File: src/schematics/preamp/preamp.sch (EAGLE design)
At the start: 33 parts

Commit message: Added input protection resistor to preamp
Ah input resistor was added to preamp inputs, so that short circuits of
clamping diodes won't hurt the connected device outputs.

Andrea Zoppi
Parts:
- added R17, R18: 1k, rcl:R-US_0204/5
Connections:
- new net N$3: C3.-, D3.A, D4.C, R18.2, R2.2
- new net N$8: C2.-, D1.A, D2.C, R17.2, R4.2
- net INA: now also R17.1; no longer C2.-, D1.A, D2.C, R4.2
- net INB: now also R18.1; no longer C3.-, D3.A, D4.C, R2.2
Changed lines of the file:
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@@
 <part name="C8" library="rcl" deviceset="C-US" device="050-025X075" value="47n"/>
 <part name="C1" library="rcl" deviceset="CPOL-US" device="E2-4" value="1u5"/>
+<part name="R17" library="rcl" deviceset="R-US_" device="0204/5" value="1k"/>
+<part name="R18" library="rcl" deviceset="R-US_" device="0204/5" value="1k"/>
 </parts>
 <sheets>
@@
 <instance part="C8" gate="G$1" x="7.62" y="144.78"/>
 <instance part="C1" gate="G$1" x="17.78" y="144.78"/>
+<instance part="R17" gate="G$1" x="-2.54" y="96.52"/>
+<instance part="R18" gate="G$1" x="-2.54" y="50.8"/>
 </instances>
 <busses>
@@
 <net name="INA" class="0">
 <segment>
-<pinref part="R4" gate="G$1" pin="2"/>
-<wire x1="12.7" y1="96.52" x2="5.08" y2="96.52" width="0.1524" layer="91"/>
-<wire x1="5.08" y1="96.52" x2="5.08" y2="93.98" width="0.1524" layer="91"/>
-<wire x1="12.7" y1="91.44" x2="12.7" y2="96.52" width="0.1524" layer="91"/>
-<wire x1="12.7" y1="101.6" x2="12.7" y2="96.52" width="0.1524" layer="91"/>
-<junction x="12.7" y="96.52"/>
-<wire x1="-5.08" y1="96.52" x2="5.08" y2="96.52" width="0.1524" layer="91"/>
-<junction x="5.08" y="96.52"/>
-<label x="-2.54" y="96.52" size="1.778" layer="95"/>
-<pinref part="D1" gate="G$1" pin="A"/>
-<pinref part="D2" gate="G$1" pin="C"/>
-<wire x1="20.32" y1="96.52" x2="12.7" y2="96.52" width="0.1524" layer="91"/>
-<pinref part="C2" gate="G$1" pin="-"/>
+<pinref part="R17" gate="G$1" pin="1"/>
+<wire x1="-7.62" y1="96.52" x2="-17.78" y2="96.52" width="0.1524" layer="91"/>
+<label x="-15.24" y="96.52" size="1.778" layer="95"/>
 </segment>
 </net>
@@
 <net name="INB" class="0">
 <segment>
-<wire x1="12.7" y1="55.88" x2="12.7" y2="50.8" width="0.1524" layer="91"/>
-<pinref part="R2" gate="G$1" pin="2"/>
-<wire x1="12.7" y1="50.8" x2="12.7" y2="45.72" width="0.1524" layer="91"/>
-<wire x1="12.7" y1="50.8" x2="5.08" y2="50.8" width="0.1524" layer="91"/>
-<wire x1="5.08" y1="50.8" x2="5.08" y2="48.26" width="0.1524" layer="91"/>
-<junction x="12.7" y="50.8"/>
-<wire x1="-5.08" y1="50.8" x2="5.08" y2="50.8" width="0.1524" layer="91"/>
-<junction x="5.08" y="50.8"/>
-<label x="-2.54" y="50.8" size="1.778" layer="95"/>
-<pinref part="D3" gate="G$1" pin="A"/>
-<pinref part="D4" gate="G$1" pin="C"/>
-<pinref part="C3" gate="G$1" pin="-"/>
-<wire x1="20.32" y1="50.8" x2="12.7" y2="50.8" width="0.1524" layer="91"/>
+<pinref part="R18" gate="G$1" pin="1"/>
+<wire x1="-7.62" y1="50.8" x2="-17.78" y2="50.8" width="0.1524" layer="91"/>
+<label x="-15.24" y="50.8" size="1.778" layer="95"/>
 </segment>
 </net>
@@
 </segment>
 </net>
+<net name="N$3" class="0">
+<segment>
+<pinref part="R18" gate="G$1" pin="2"/>
+<pinref part="C3" gate="G$1" pin="-"/>
+<wire x1="2.54" y1="50.8" x2="5.08" y2="50.8" width="0.1524" layer="91"/>
+<pinref part="D3" gate="G$1" pin="A"/>
+<wire x1="5.08" y1="50.8" x2="12.7" y2="50.8" width="0.1524" layer="91"/>
+<wire x1="12.7" y1="50.8" x2="20.32" y2="50.8" width="0.1524" layer="91"/>
+<wire x1="12.7" y1="55.88" x2="12.7" y2="50.8" width="0.1524" layer="91"/>
+<pinref part="D4" gate="G$1" pin="C"/>
+<wire x1="12.7" y1="45.72" x2="12.7" y2="50.8" width="0.1524" layer="91"/>
+<pinref part="R2" gate="G$1" pin="2"/>
+<wire x1="5.08" y1="48.26" x2="5.08" y2="50.8" width="0.1524" layer="91"/>
+<junction x="5.08" y="50.8"/>
+<junction x="12.7" y="50.8"/>
+</segment>
+</net>
+<net name="N$8" class="0">
+<segment>
+<pinref part="R17" gate="G$1" pin="2"/>
+<pinref part="C2" gate="G$1" pin="-"/>
+<wire x1="2.54" y1="96.52" x2="5.08" y2="96.52" width="0.1524" layer="91"/>
+<pinref part="D1" gate="G$1" pin="A"/>
+<wire x1="5.08" y1="96.52" x2="12.7" y2="96.52" width="0.1524" layer="91"/>
+<wire x1="12.7" y1="96.52" x2="20.32" y2="96.52" width="0.1524" layer="91"/>
+<wire x1="12.7" y1="101.6" x2="12.7" y2="96.52" width="0.1524" layer="91"/>
+<pinref part="D2" gate="G$1" pin="C"/>
+<wire x1="12.7" y1="91.44" x2="12.7" y2="96.52" width="0.1524" layer="91"/>
+<pinref part="R4" gate="G$1" pin="2"/>
+<wire x1="5.08" y1="93.98" x2="5.08" y2="96.52" width="0.1524" layer="91"/>
+<junction x="5.08" y="96.52"/>
+<junction x="12.7" y="96.52"/>
+</segment>
+</net>

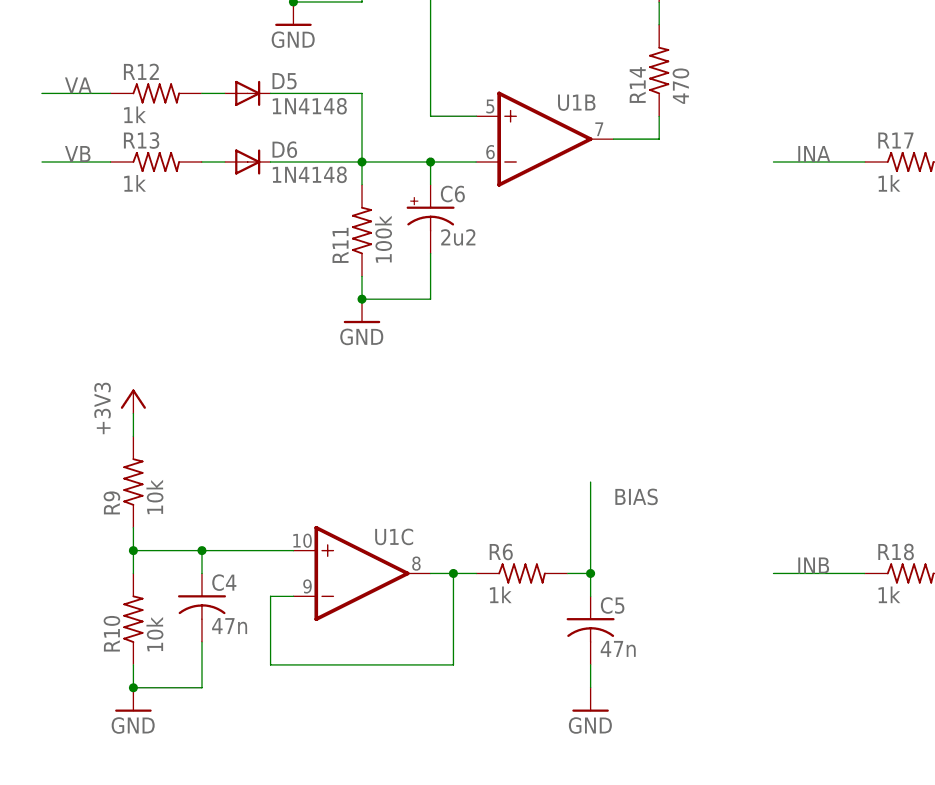
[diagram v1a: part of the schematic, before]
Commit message: Added double RCA connector to preamp module
Andrea Zoppi
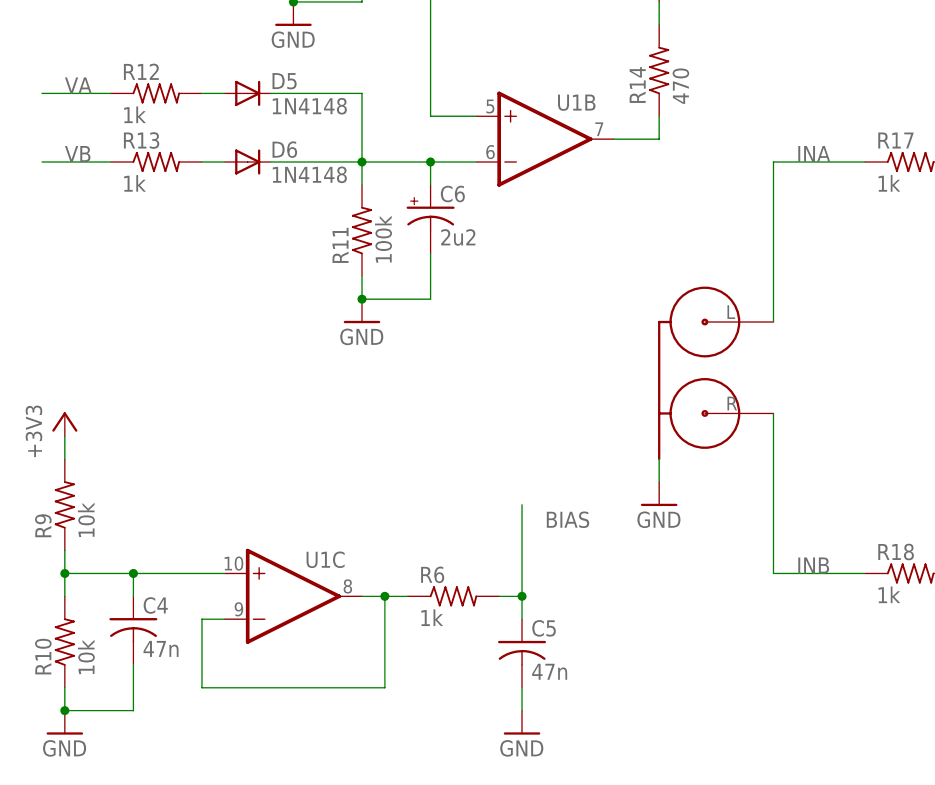
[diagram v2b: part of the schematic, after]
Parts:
- added RCA1: RCA-2V, con_local:RCA-2V
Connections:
- net GND: now also RCA1.SHIELD
- net INA: now also RCA1.L
- net INB: now also RCA1.R
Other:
- moved on the sheet: C4, C5, R10, R6, R9, U1C
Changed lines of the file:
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@@
 <part name="R17" library="rcl" deviceset="R-US_" device="0204/5" value="1k"/>
 <part name="R18" library="rcl" deviceset="R-US_" device="0204/5" value="1k"/>
+<part name="RCA1" library="con_local" deviceset="RCA-2V" device=""/>
+<part name="GND9" library="supply1" deviceset="GND" device=""/>
 </parts>
 <sheets>
@@
 <instance part="GND2" gate="1" x="-71.12" y="111.76"/>
 <instance part="GND4" gate="1" x="12.7" y="33.02"/>
-<instance part="C4" gate="G$1" x="-81.28" y="48.26"/>
-<instance part="C5" gate="G$1" x="-38.1" y="45.72"/>
+<instance part="C4" gate="G$1" x="-88.9" y="45.72"/>
+<instance part="C5" gate="G$1" x="-45.72" y="43.18"/>
 <instance part="R2" gate="G$1" x="5.08" y="43.18" rot="R90"/>
 <instance part="R3" gate="G$1" x="33.02" y="43.18" rot="R90"/>
 <instance part="R4" gate="G$1" x="5.08" y="88.9" rot="R90"/>
 <instance part="R5" gate="G$1" x="33.02" y="88.9" rot="R90"/>
-<instance part="R6" gate="G$1" x="-45.72" y="50.8"/>
+<instance part="R6" gate="G$1" x="-53.34" y="48.26"/>
 <instance part="R7" gate="G$1" x="68.58" y="53.34"/>
 <instance part="R8" gate="G$1" x="68.58" y="99.06"/>
 <instance part="GND3" gate="1" x="12.7" y="78.74"/>
-<instance part="GND5" gate="1" x="-38.1" y="35.56"/>
-<instance part="R9" gate="G$1" x="-88.9" y="60.96" rot="R90"/>
-<instance part="R10" gate="G$1" x="-88.9" y="45.72" rot="R90"/>
-<instance part="+3V5" gate="G$1" x="-88.9" y="71.12"/>
-<instance part="GND6" gate="1" x="-88.9" y="35.56"/>
+<instance part="GND5" gate="1" x="-45.72" y="33.02"/>
+<instance part="R9" gate="G$1" x="-96.52" y="58.42" rot="R90"/>
+<instance part="R10" gate="G$1" x="-96.52" y="43.18" rot="R90"/>
+<instance part="+3V5" gate="G$1" x="-96.52" y="68.58"/>
+<instance part="GND6" gate="1" x="-96.52" y="33.02"/>
 <instance part="GND7" gate="1" x="78.74" y="149.86"/>
 <instance part="+3V6" gate="G$1" x="71.12" y="157.48"/>
@@
 <instance part="U1" gate="A" x="50.8" y="99.06"/>
 <instance part="U1" gate="B" x="-43.18" y="99.06"/>
-<instance part="U1" gate="C" x="-63.5" y="50.8"/>
+<instance part="U1" gate="C" x="-71.12" y="48.26"/>
 <instance part="U1" gate="D" x="50.8" y="53.34"/>
 <instance part="U1" gate="P" x="27.94" y="142.24"/>
@@
 <instance part="R17" gate="G$1" x="-2.54" y="96.52"/>
 <instance part="R18" gate="G$1" x="-2.54" y="50.8"/>
+<instance part="RCA1" gate="G$1" x="-25.4" y="73.66"/>
+<instance part="GND9" gate="1" x="-30.48" y="58.42"/>
 </instances>
 <busses>
@@
 <pinref part="+3V5" gate="G$1" pin="+3V3"/>
 <pinref part="R9" gate="G$1" pin="2"/>
-<wire x1="-88.9" y1="68.58" x2="-88.9" y2="66.04" width="0.1524" layer="91"/>
+<wire x1="-96.52" y1="66.04" x2="-96.52" y2="63.5" width="0.1524" layer="91"/>
 </segment>
 <segment>
@@
 <pinref part="C5" gate="G$1" pin="2"/>
 <pinref part="GND5" gate="1" pin="GND"/>
-<wire x1="-38.1" y1="38.1" x2="-38.1" y2="40.64" width="0.1524" layer="91"/>
+<wire x1="-45.72" y1="35.56" x2="-45.72" y2="38.1" width="0.1524" layer="91"/>
 </segment>
 <segment>
 <pinref part="C4" gate="G$1" pin="2"/>
-<wire x1="-81.28" y1="43.18" x2="-81.28" y2="38.1" width="0.1524" layer="91"/>
+<wire x1="-88.9" y1="40.64" x2="-88.9" y2="35.56" width="0.1524" layer="91"/>
 <pinref part="R10" gate="G$1" pin="1"/>
-<wire x1="-81.28" y1="38.1" x2="-88.9" y2="38.1" width="0.1524" layer="91"/>
-<wire x1="-88.9" y1="38.1" x2="-88.9" y2="40.64" width="0.1524" layer="91"/>
+<wire x1="-88.9" y1="35.56" x2="-96.52" y2="35.56" width="0.1524" layer="91"/>
+<wire x1="-96.52" y1="35.56" x2="-96.52" y2="38.1" width="0.1524" layer="91"/>
 <pinref part="GND6" gate="1" pin="GND"/>
-<junction x="-88.9" y="38.1"/>
+<junction x="-96.52" y="35.56"/>
 </segment>
 <segment>
@@
 <wire x1="17.78" y1="139.7" x2="17.78" y2="132.08" width="0.1524" layer="91"/>
 </segment>
+<segment>
+<pinref part="GND9" gate="1" pin="GND"/>
+<pinref part="RCA1" gate="G$1" pin="SHIELD"/>
+<wire x1="-30.48" y1="60.96" x2="-30.48" y2="63.5" width="0.1524" layer="91"/>
+</segment>
 </net>
 <net name="N$1" class="0">
 <segment>
 <pinref part="C4" gate="G$1" pin="1"/>
-<wire x1="-81.28" y1="50.8" x2="-81.28" y2="53.34" width="0.1524" layer="91"/>
+<wire x1="-88.9" y1="48.26" x2="-88.9" y2="50.8" width="0.1524" layer="91"/>
 <pinref part="R9" gate="G$1" pin="1"/>
 <pinref part="R10" gate="G$1" pin="2"/>
-<wire x1="-88.9" y1="55.88" x2="-88.9" y2="53.34" width="0.1524" layer="91"/>
-<wire x1="-88.9" y1="53.34" x2="-88.9" y2="50.8" width="0.1524" layer="91"/>
-<wire x1="-88.9" y1="53.34" x2="-81.28" y2="53.34" width="0.1524" layer="91"/>
-<junction x="-88.9" y="53.34"/>
-<wire x1="-81.28" y1="53.34" x2="-71.12" y2="53.34" width="0.1524" layer="91"/>
-<junction x="-81.28" y="53.34"/>
+<wire x1="-96.52" y1="53.34" x2="-96.52" y2="50.8" width="0.1524" layer="91"/>
+<wire x1="-96.52" y1="50.8" x2="-96.52" y2="48.26" width="0.1524" layer="91"/>
+<wire x1="-96.52" y1="50.8" x2="-88.9" y2="50.8" width="0.1524" layer="91"/>
+<junction x="-96.52" y="50.8"/>
+<wire x1="-88.9" y1="50.8" x2="-78.74" y2="50.8" width="0.1524" layer="91"/>
+<junction x="-88.9" y="50.8"/>
 <pinref part="U1" gate="C" pin="+IN"/>
 </segment>
@@
 <wire x1="-7.62" y1="96.52" x2="-17.78" y2="96.52" width="0.1524" layer="91"/>
 <label x="-15.24" y="96.52" size="1.778" layer="95"/>
+<pinref part="RCA1" gate="G$1" pin="L"/>
+<wire x1="-17.78" y1="78.74" x2="-17.78" y2="96.52" width="0.1524" layer="91"/>
 </segment>
 </net>
@@
 <pinref part="R6" gate="G$1" pin="2"/>
 <pinref part="C5" gate="G$1" pin="1"/>
-<wire x1="-38.1" y1="50.8" x2="-38.1" y2="48.26" width="0.1524" layer="91"/>
-<wire x1="-38.1" y1="50.8" x2="-38.1" y2="60.96" width="0.1524" layer="91"/>
-<junction x="-38.1" y="50.8"/>
-<wire x1="-38.1" y1="50.8" x2="-40.64" y2="50.8" width="0.1524" layer="91"/>
-<label x="-35.56" y="58.42" size="1.778" layer="95"/>
+<wire x1="-45.72" y1="48.26" x2="-45.72" y2="45.72" width="0.1524" layer="91"/>
+<wire x1="-45.72" y1="48.26" x2="-45.72" y2="58.42" width="0.1524" layer="91"/>
+<junction x="-45.72" y="48.26"/>
+<wire x1="-45.72" y1="48.26" x2="-48.26" y2="48.26" width="0.1524" layer="91"/>
+<label x="-43.18" y="55.88" size="1.778" layer="95"/>
 </segment>
 <segment>
@@
 <wire x1="-7.62" y1="50.8" x2="-17.78" y2="50.8" width="0.1524" layer="91"/>
 <label x="-15.24" y="50.8" size="1.778" layer="95"/>
+<wire x1="-17.78" y1="50.8" x2="-17.78" y2="68.58" width="0.1524" layer="91"/>
+<pinref part="RCA1" gate="G$1" pin="R"/>
 </segment>
 </net>
@@
 <net name="N$7" class="0">
 <segment>
-<wire x1="-73.66" y1="48.26" x2="-73.66" y2="40.64" width="0.1524" layer="91"/>
-<wire x1="-73.66" y1="40.64" x2="-53.34" y2="40.64" width="0.1524" layer="91"/>
-<wire x1="-53.34" y1="40.64" x2="-53.34" y2="50.8" width="0.1524" layer="91"/>
+<wire x1="-81.28" y1="45.72" x2="-81.28" y2="38.1" width="0.1524" layer="91"/>
+<wire x1="-81.28" y1="38.1" x2="-60.96" y2="38.1" width="0.1524" layer="91"/>
+<wire x1="-60.96" y1="38.1" x2="-60.96" y2="48.26" width="0.1524" layer="91"/>
 <pinref part="R6" gate="G$1" pin="1"/>
-<wire x1="-50.8" y1="50.8" x2="-53.34" y2="50.8" width="0.1524" layer="91"/>
-<wire x1="-73.66" y1="48.26" x2="-71.12" y2="48.26" width="0.1524" layer="91"/>
-<wire x1="-55.88" y1="50.8" x2="-53.34" y2="50.8" width="0.1524" layer="91"/>
-<junction x="-53.34" y="50.8"/>
+<wire x1="-58.42" y1="48.26" x2="-60.96" y2="48.26" width="0.1524" layer="91"/>
+<wire x1="-81.28" y1="45.72" x2="-78.74" y2="45.72" width="0.1524" layer="91"/>
+<wire x1="-63.5" y1="48.26" x2="-60.96" y2="48.26" width="0.1524" layer="91"/>
+<junction x="-60.96" y="48.26"/>
 <pinref part="U1" gate="C" pin="-IN"/>
 <pinref part="U1" gate="C" pin="OUT"/>

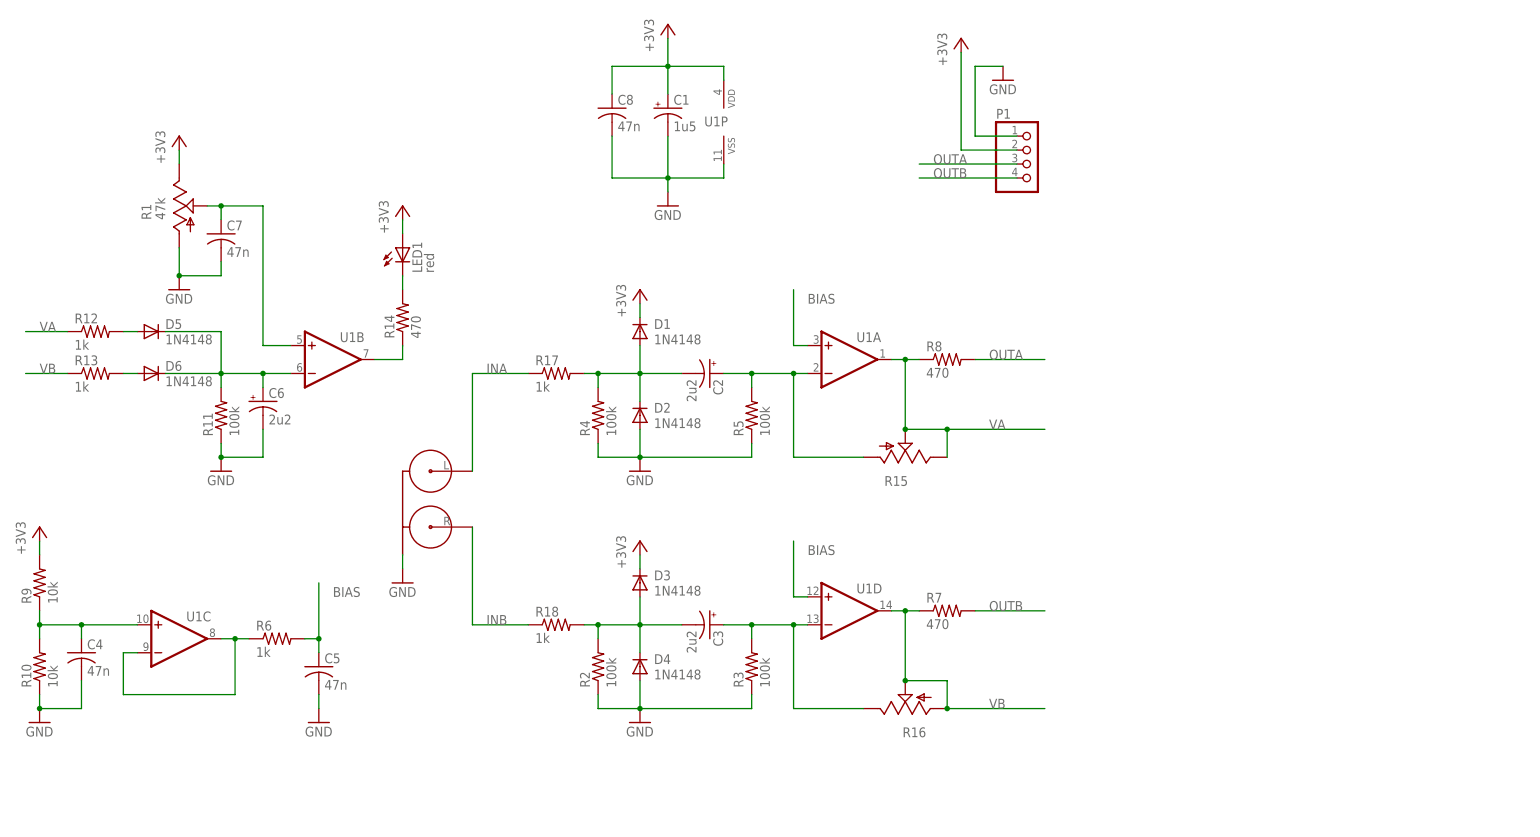
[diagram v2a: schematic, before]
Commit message: Trimmable preamp positive reference
The preamp positive voltage reference is now trimmable, so that it can be
calibrated in order to reduce misalignments with the main board's internal
reference (internal DAC output of the PIC).

Preamp board schematics refactored.

Andrea Zoppi
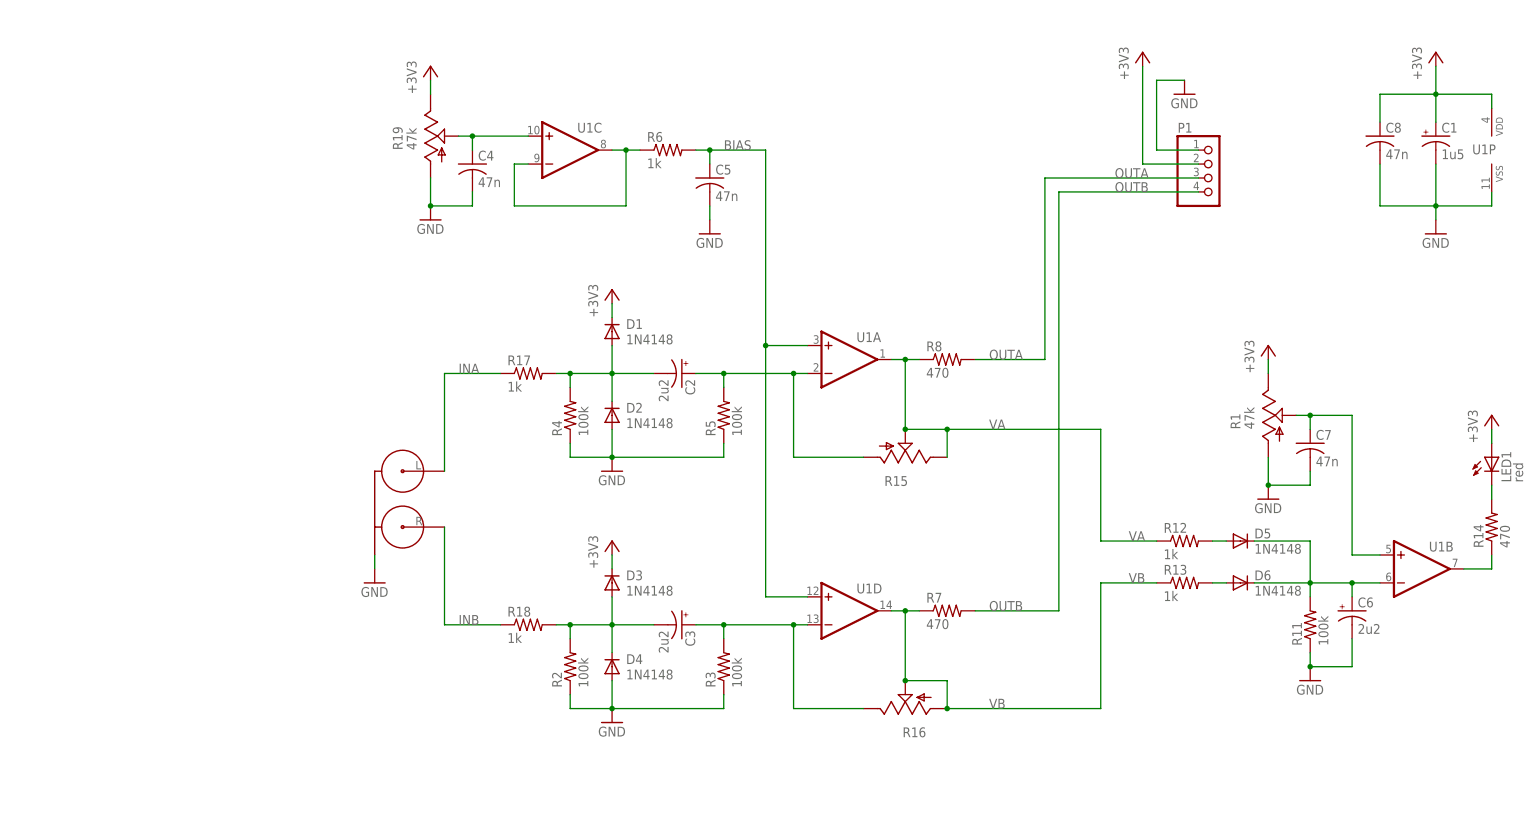
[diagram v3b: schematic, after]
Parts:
- removed R10, R9: 10k, rcl:R-US_0204/5
- added R19: 47k, pot:TRIM_US-PT-10S
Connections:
- new net N$14: R19.A
- net +3V3: now also R19.E; no longer R9.2
- net GND: no longer R10.1
- net N$1: now also R19.S; no longer R10.2, R9.1
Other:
- moved on the sheet: C1, C2, C3, C4, C5, C6, C7, C8, D1, D2, D3, D4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
